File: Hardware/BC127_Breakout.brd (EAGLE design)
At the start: 63.5 x 30.5 mm, 37 parts, among them Q1 MOSFET-NCHANNELBSS138, Q2 MOSFET-NCHANNELBSS138, Q3 MMBT4403, U2 MIC5219 3.3V

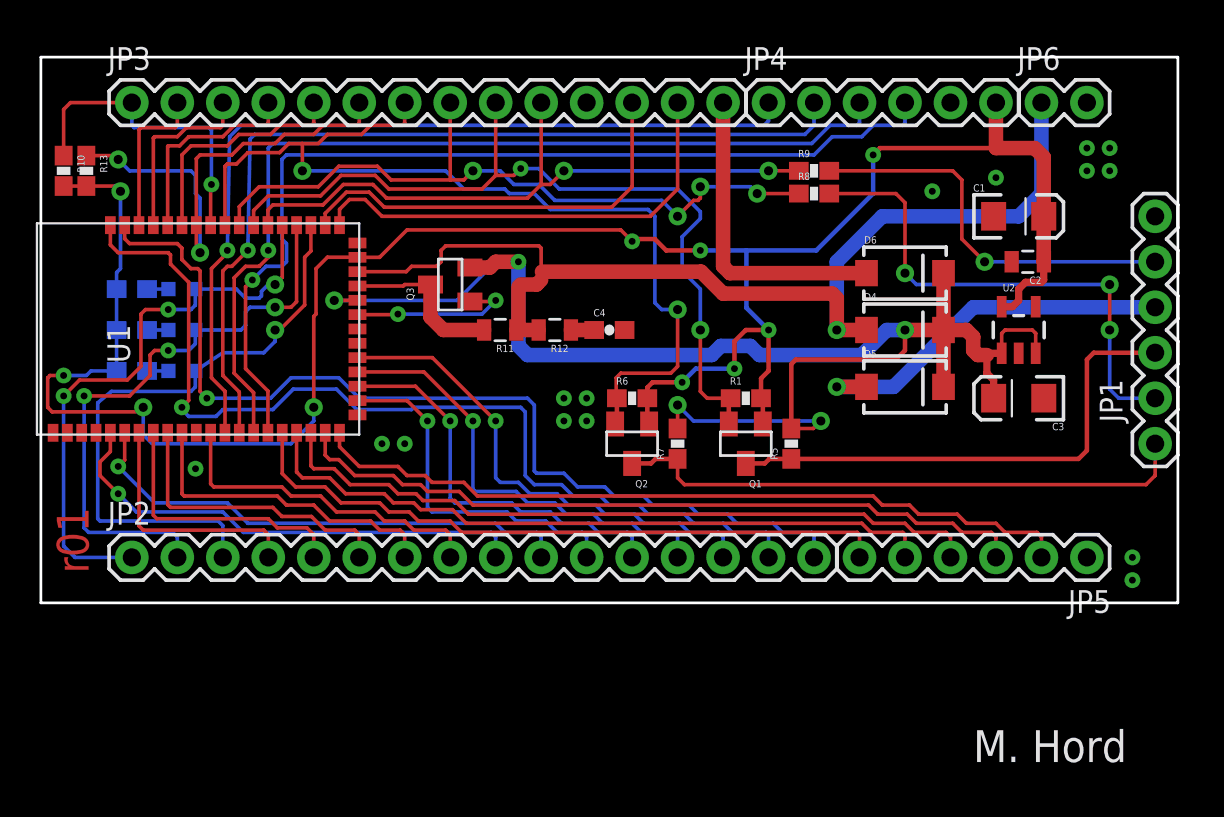
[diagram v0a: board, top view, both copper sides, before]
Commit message: Feedback from review implemented. Proto.
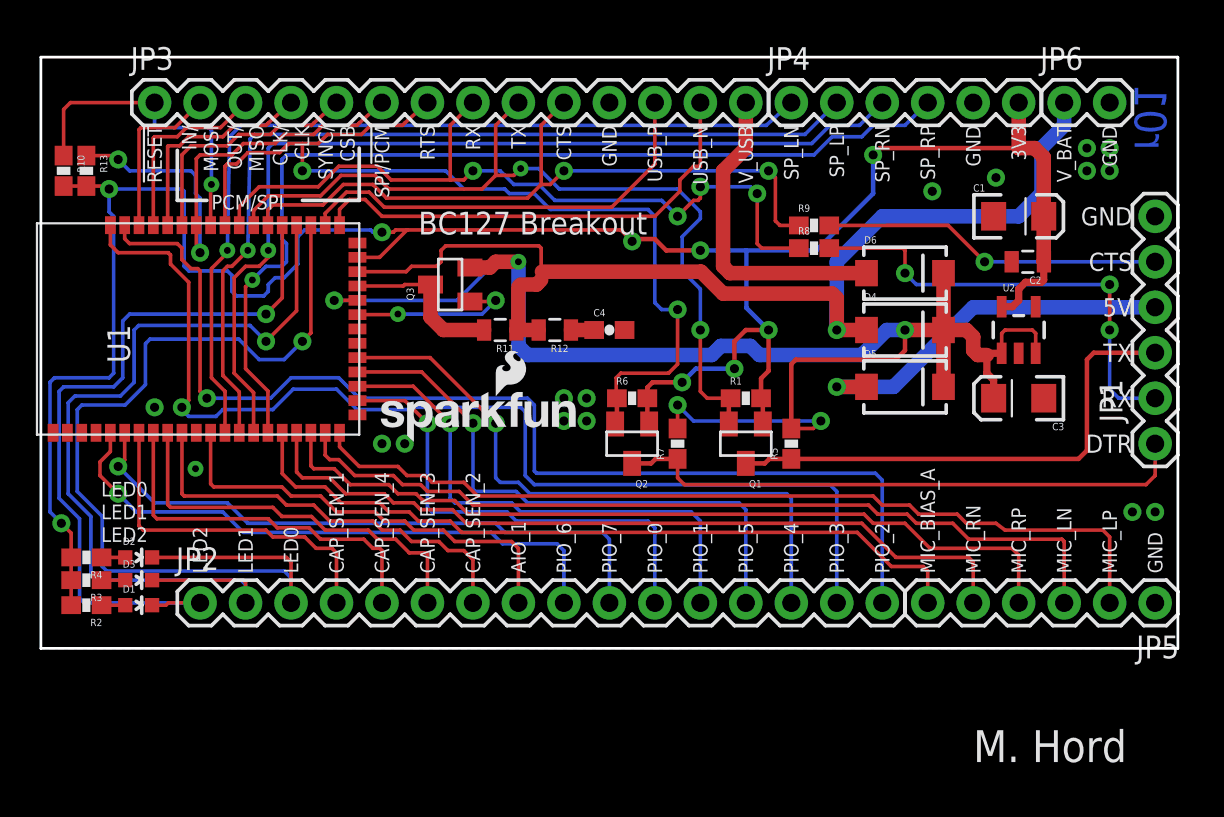
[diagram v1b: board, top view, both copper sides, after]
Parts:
- added LOGO3: SFE_LOGO_NAME_FLAME.1_INCH, SparkFun-Aesthetics:SFE_LOGO_NAME_FLAME_.1
- moved R2 17.8 mm to (2.54, -0.13), flipped to the top, turned to 180 degrees
- moved D1 17.8 mm to (5.46, -0.13), flipped to the top, turned to 270 degrees
- moved R3 14.2 mm to (2.54, 1.27), flipped to the top, turned to 180 degrees
- moved D3 14.2 mm to (5.46, 1.27), flipped to the top, turned to 270 degrees
- moved U1 10.8 mm to (8.78, 15.3)
- moved R4 10.7 mm to (2.54, 2.54), flipped to the top, turned to 180 degrees
- moved D2 10.7 mm to (5.46, 2.54), flipped to the top, turned to 270 degrees
- moved JP2 4.58 mm to (8.89, 0.00)
- moved JP5 4.58 mm to (62.2, 0.00)
- moved R8 3.05 mm to (43.2, 19.8)
- moved R9 3.05 mm to (43.2, 21.1)
- moved JP3 1.27 mm to (6.35, 27.9)
- moved JP4 1.27 mm to (41.9, 27.9)
- moved JP6 1.27 mm to (57.1, 27.9)
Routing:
- net LED_0: track 34.6 -> 54.8 mm
- net LED_1: track 33.8 -> 48.6 mm, vias 3 -> 1
- net LED_2: track 33.1 -> 42.1 mm, vias 3 -> 1
- net PIO_2: track 54.8 -> 62.9 mm
- net PIO_3: track 54.3 -> 62.1 mm
- net PIO_4: track 27.6 -> 35.1 mm
- net PIO_5: track 25.1 -> 32.2 mm
- net 3.3V: track 125.2 -> 132.2 mm, vias 10 -> 9
- net PIO_1: track 22.5 -> 29.3 mm
- net PIO_0: track 19.9 -> 26.5 mm
- net MIC_LP: track 43.2 -> 49.5 mm
- net PIO_7: track 28.4 -> 34.7 mm
- net MIC_LN: track 41.7 -> 47.9 mm
- net PIO_6: track 27.3 -> 33.2 mm
- net AIO_1: track 18.7 -> 24.6 mm
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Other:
- board size 63.5 x 30.5 mm -> 63.5 x 33 mm
- board text added: "CAP_SEN_1"
- board text added: "CAP_SEN_2"
- board text added: "CAP_SEN_3"
- board text added: "CAP_SEN_4"
- board text added: "CLK/ CLK"
- board text added: "IN/ MOSI"
- board text added: "OUT/ MISO"
- board text added: "PCM/SPI"
- board text added: "SP_LN"
- board text added: "SP_LP"
- board text added: "SP_RN"
- board text added: "SP_RP"
- board text added: "SYNC/ CSB"

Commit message: Ready for 2nd protos
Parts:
- JP3: value M14 -> M15; device SparkFun-Connectors:1X14 -> SparkFun-Connectors:1X15
- LOGO3: value SFE_LOGO_NAME_FLAME.1_INCH -> SFE_LOGO_NAME.1_INCH; device SparkFun-Aesthetics:SFE_LOGO_NAME_FLAME_.1 -> SparkFun-Aesthetics:SFE_LOGO_NAME_.1
- moved JP4 2.54 mm to (44.5, 27.9)
- moved JP6 2.54 mm to (59.7, 27.9)
- moved LOGO3 1.91 mm to (18.7, 10.8)
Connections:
- net VREGEN: now also JP3.15
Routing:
- net VREGEN: track 0.00 -> 41.8 mm, vias 0 -> 4
- net SPKR_LP: track 51.1 -> 54.0 mm
- net SPKR_LN: track 49.3 -> 52.0 mm
- net SPKR_RP: track 54.7 -> 57.3 mm
- net SPKR_RN: track 52.9 -> 55.5 mm
- net USB_N: track 26.7 -> 25.2 mm
- net V_BAT: track 61.1 -> 62.2 mm
- net 3.3V: track 132.2 -> 133.1 mm
- net TX: track 47.2 -> 46.5 mm
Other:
- board text added: "Bluetooth 2.1/4.0"
- board text added: "VREGEN"
- board text added: "r02"
- board text removed: "r01"

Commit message: Protos checked out, go for reds.
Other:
- board text added: "r10"
- board text removed: "r02"
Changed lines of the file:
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@@
 <grid distance="0.05" unitdist="inch" unit="inch" style="lines" multiple="1" display="yes" altdistance="0.005" altunitdist="inch" altunit="inch"/>
 <layers>
-<layer number="1" name="Top" color="4" fill="1" visible="no" active="yes"/>
+<layer number="1" name="Top" color="4" fill="1" visible="yes" active="yes"/>
 <layer number="2" name="Route2" color="1" fill="3" visible="no" active="yes"/>
 <layer number="15" name="Route15" color="4" fill="6" visible="no" active="yes"/>
@@
 <layer number="19" name="Unrouted" color="6" fill="1" visible="yes" active="yes"/>
 <layer number="20" name="Dimension" color="15" fill="1" visible="yes" active="yes"/>
-<layer number="21" name="tPlace" color="16" fill="1" visible="no" active="yes"/>
+<layer number="21" name="tPlace" color="16" fill="1" visible="yes" active="yes"/>
 <layer number="22" name="bPlace" color="14" fill="1" visible="yes" active="yes"/>
-<layer number="23" name="tOrigins" color="15" fill="1" visible="no" active="yes"/>
+<layer number="23" name="tOrigins" color="15" fill="1" visible="yes" active="yes"/>
 <layer number="24" name="bOrigins" color="15" fill="1" visible="yes" active="yes"/>
 <layer number="25" name="tNames" color="7" fill="1" visible="no" active="yes"/>
@@
 <layer number="43" name="vRestrict" color="2" fill="10" visible="no" active="yes"/>
 <layer number="44" name="Drills" color="7" fill="1" visible="no" active="yes"/>
-<layer number="45" name="Holes" color="7" fill="1" visible="no" active="yes"/>
+<layer number="45" name="Holes" color="7" fill="1" visible="yes" active="yes"/>
 <layer number="46" name="Milling" color="3" fill="1" visible="no" active="yes"/>
-<layer number="51" name="tDocu" color="6" fill="1" visible="no" active="yes"/>
+<layer number="51" name="tDocu" color="6" fill="1" visible="yes" active="yes"/>
 <layer number="52" name="bDocu" color="7" fill="1" visible="no" active="yes"/>
 <layer number="3" name="Route3" color="4" fill="3" visible="no" active="no"/>
@@
 <wire x1="17.78" y1="22.479" x2="17.78" y2="25.4" width="0.2032" layer="21"/>
 <text x="21.082" y="21.209" size="1.27" layer="21" font="vector" ratio="15" align="center-left">BC127 Breakout</text>
-<text x="1.397" y="25.273" size="1.778" layer="16" font="vector" ratio="15" rot="MR90">r02</text>
+<text x="1.397" y="25.273" size="1.778" layer="16" font="vector" ratio="15" rot="MR90">r10</text>
 <text x="26.924" y="16.891" size="1.27" layer="21" font="vector" ratio="15">Bluetooth 2.1/4.0</text>
 <text x="39.37" y="26.67" size="0.8128" layer="21" font="vector" ratio="15" rot="R90" align="center-right">V_USB</text>
@@
 </signal>
 </signals>
+<errors>
+</errors>
 </board>
 </drawing>
